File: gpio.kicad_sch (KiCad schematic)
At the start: 13 parts, among them J5 Conn_02x08_Odd_Even, J6 USB_9P, J7 Conn_01x04, U10 TLP172GM, U5 TLP172GM, U6 TLP172GM, U9 TLP172GM

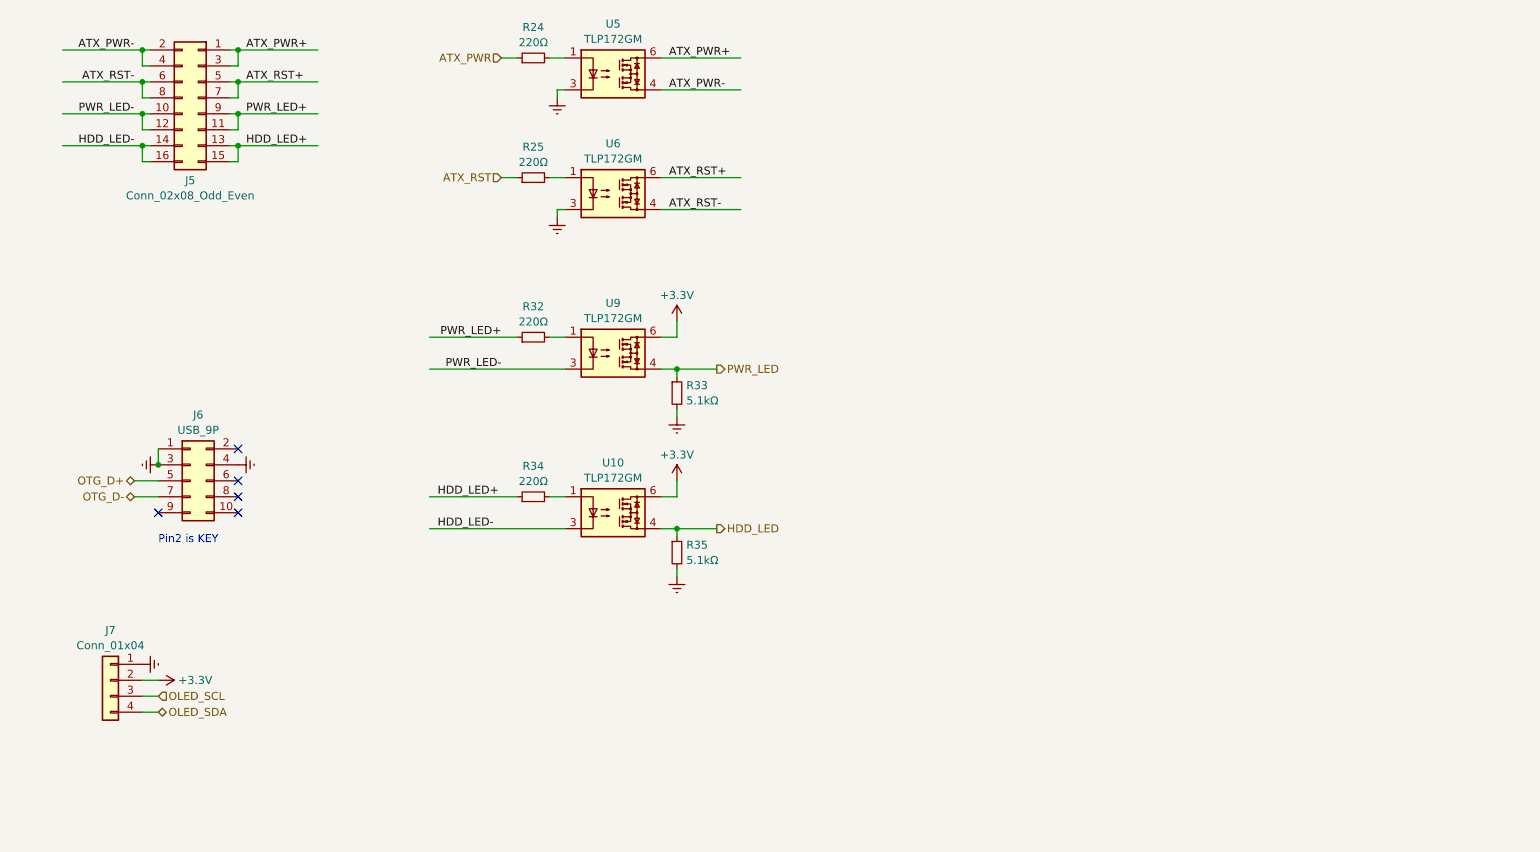
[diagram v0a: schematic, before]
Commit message: Update pcb & sch for T113 SOM
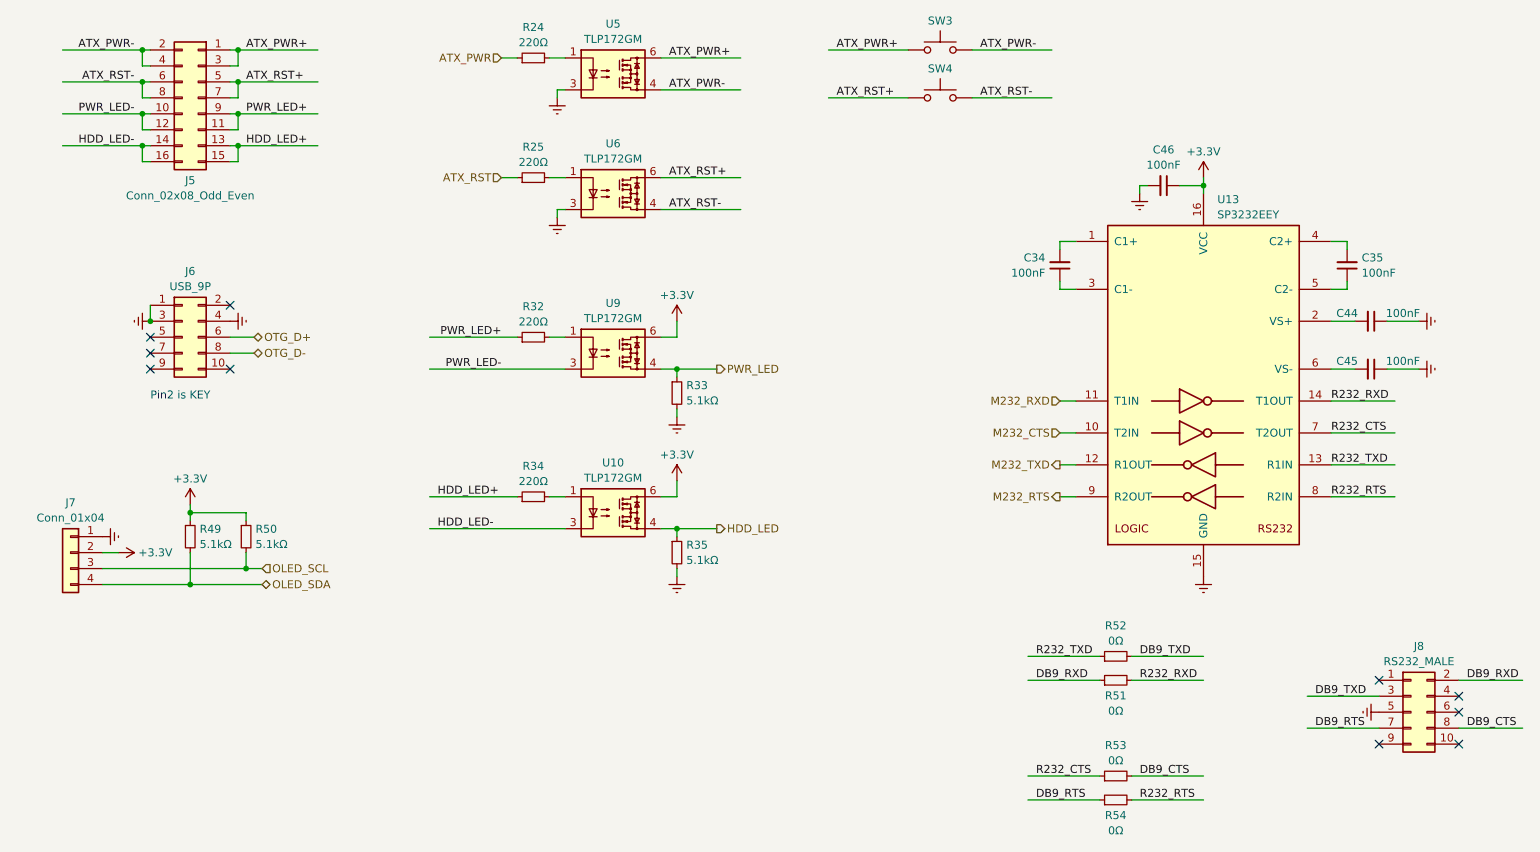
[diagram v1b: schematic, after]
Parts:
- added C34, C35, C44, C45, C46: 100nF, Capacitor_SMD:C_0402_1005Metric, symbol Device:C_Small
- added J8: RS232_MALE, easyeda2kicad:IDC-SMD_10P-P2.54-V-R2-C5-S9.50, symbol Connector_Generic:Conn_02x05_Odd_Even
- added R49, R50: 5.1kΩ, Resistor_SMD:R_0402_1005Metric, symbol Device:R_Small
- added R51, R52, R53, R54: 0Ω, Resistor_SMD:R_0402_1005Metric, symbol Device:R_Small
- added SW3, SW4: TS-1187A, Button_Switch_SMD:SW_Push_1P1T_XKB_TS-1187A, symbol Switch:SW_Push
- added U13: SP3232EEY, Package_SO:TSSOP-16_4.4x5mm_P0.65mm, symbol Interface_UART:MAX3232
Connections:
- net +3.3V: now also C46.1, R49.1, R50.1, U13.16 (VCC)
- net ATX_PWR+: now also SW3.1
- net ATX_PWR-: now also SW3.2
- net ATX_RST+: now also SW4.1
- net ATX_RST-: now also SW4.2
- net Earth: now also C44.1, C45.1, C46.2, J8.5 (Pin_5), U13.15 (GND)
- net OLED_SCL: now also R50.2
- net OLED_SDA: now also R49.2
- net OTG_D+: now also J6.6 (Pin_6); no longer J6.5 (Pin_5)
- net OTG_D-: now also J6.8 (Pin_8); no longer J6.7 (Pin_7)
- new net: C45.2, U13.6 (VS-)
- new net: C34.2, U13.1 (C1+)
- new net: C44.2, U13.2 (VS+)
- new net: C34.1, U13.3 (C1-)
- new net: C35.2, U13.4 (C2+)
- new net: C35.1, U13.5 (C2-)
- new net DB9_CTS: J8.8 (Pin_8), R53.2
- new net DB9_RTS: J8.7 (Pin_7), R54.1
- new net DB9_RXD: J8.2 (Pin_2), R51.1
- new net DB9_TXD: J8.3 (Pin_3), R52.2
- new net M232_CTS: U13.10 (T2IN)
- new net M232_RTS: U13.9 (R2OUT)
- new net M232_RXD: U13.11 (T1IN)
- new net M232_TXD: U13.12 (R1OUT)
- new net R232_CTS: R53.1, U13.7 (T2OUT)
- new net R232_RTS: R54.2, U13.8 (R2IN)
- new net R232_RXD: R51.2, U13.14 (T1OUT)
- new net R232_TXD: R52.1, U13.13 (R1IN)
- no-connect marks 5 -> 10
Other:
- moved on the sheet: J6, J7

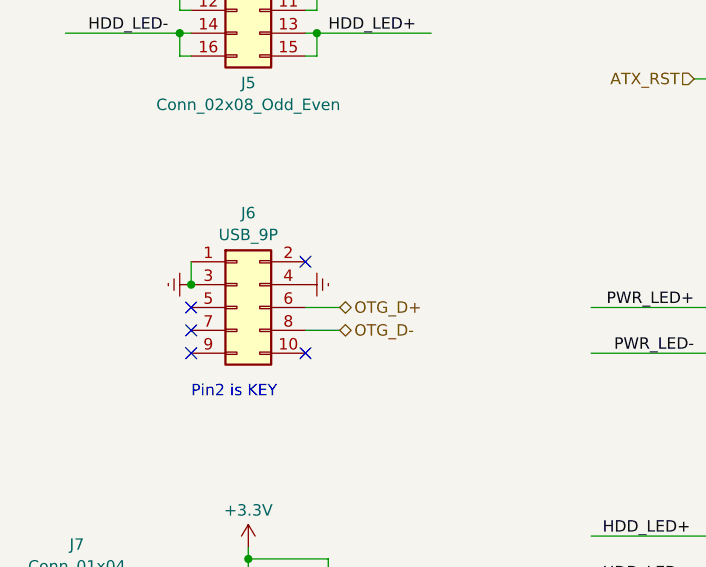
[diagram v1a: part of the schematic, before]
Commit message: Fix MS2109 symbol power pins, initial v1 release
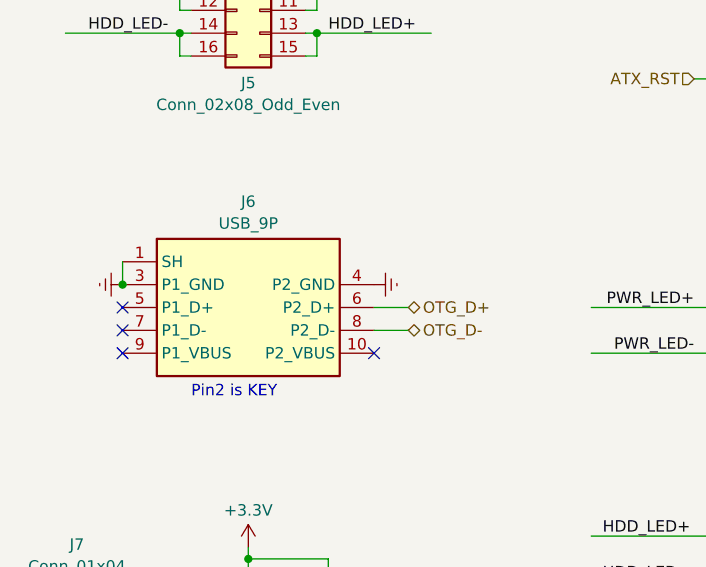
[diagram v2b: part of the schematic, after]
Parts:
- J6: symbol Connector_Generic:Conn_02x05_Odd_Even -> tukvm:PinHeader_USB_2.0_9Pin
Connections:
- no-connect marks 10 -> 9
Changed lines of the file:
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@@
 	(paper "A4")
 	(junction
-		(at 49.53 72.39)
-		(diameter 0)
-		(color 0 0 0 0)
-	)
-	(junction
 		(at 63.5 34.29)
 		(diameter 0)
@@
 	)
 	(junction
+		(at 41.91 72.39)
+		(diameter 0)
+		(color 0 0 0 0)
+	)
+	(junction
 		(at 48.26 29.21)
 		(diameter 0)
@@
 	)
 	(no_connect
-		(at 62.23 69.85)
-	)
-	(no_connect
 		(at 257.81 132.08)
 	)
 	(no_connect
-		(at 62.23 80.01)
+		(at 69.85 80.01)
 	)
 	(no_connect
@@
 	)
 	(no_connect
-		(at 49.53 80.01)
+		(at 41.91 80.01)
 	)
 	(no_connect
@@
 	)
 	(no_connect
-		(at 49.53 74.93)
+		(at 41.91 74.93)
 	)
 	(no_connect
@@
 	)
 	(no_connect
-		(at 49.53 77.47)
+		(at 41.91 77.47)
 	)
 	(wire
@@
 	(wire
 		(pts
-			(xy 49.53 69.85) (xy 49.53 72.39)
+			(xy 41.91 69.85) (xy 41.91 72.39)
 		)
 		(stroke
@@
 	(wire
 		(pts
-			(xy 66.04 74.93) (xy 62.23 74.93)
+			(xy 73.66 74.93) (xy 69.85 74.93)
 		)
 		(stroke
@@
 	(wire
 		(pts
-			(xy 66.04 77.47) (xy 62.23 77.47)
+			(xy 73.66 77.47) (xy 69.85 77.47)
 		)
 		(stroke
@@
 	(hierarchical_label "OTG_D-"
 		(shape bidirectional)
-		(at 66.04 77.47 0)
+		(at 73.66 77.47 0)
 		(fields_autoplaced yes)
 		(effects
@@
 	(hierarchical_label "OTG_D+"
 		(shape bidirectional)
-		(at 66.04 74.93 0)
+		(at 73.66 74.93 0)
 		(fields_autoplaced yes)
 		(effects
@@
 	(symbol
 		(lib_id "power:Earth")
-		(at 62.23 72.39 90)
+		(at 69.85 72.39 90)
 		(unit 1)
 		(exclude_from_sim no)
@@
 		(dnp no)
 		(property "Reference" "#PWR081"
-			(at 68.58 72.39 0)
+			(at 76.2 72.39 0)
 			(effects
 				(font
@@
 		)
 		(property "Value" "Earth"
-			(at 66.04 72.39 0)
+			(at 73.66 72.39 0)
 			(effects
 				(font
@@
 		)
 		(property "Footprint" ""
-			(at 62.23 72.39 0)
+			(at 69.85 72.39 0)
 			(effects
 				(font
@@
 		)
 		(property "Datasheet" "~"
-			(at 62.23 72.39 0)
+			(at 69.85 72.39 0)
 			(effects
 				(font
@@
 		)
 		(property "Description" ""
-			(at 62.23 72.39 0)
+			(at 69.85 72.39 0)
 			(effects
 				(font
@@
 	(symbol
 		(lib_id "power:Earth")
-		(at 49.53 72.39 270)
+		(at 41.91 72.39 270)
 		(unit 1)
 		(exclude_from_sim no)
@@
 		(dnp no)
 		(property "Reference" "#PWR079"
-			(at 43.18 72.39 0)
+			(at 35.56 72.39 0)
 			(effects
 				(font
@@
 		)
 		(property "Value" "Earth"
-			(at 45.72 72.39 0)
+			(at 38.1 72.39 0)
 			(effects
 				(font
@@
 		)
 		(property "Footprint" ""
-			(at 49.53 72.39 0)
+			(at 41.91 72.39 0)
 			(effects
 				(font
@@
 		)
 		(property "Datasheet" "~"
-			(at 49.53 72.39 0)
+			(at 41.91 72.39 0)
 			(effects
 				(font
@@
 		)
 		(property "Description" ""
-			(at 49.53 72.39 0)
+			(at 41.91 72.39 0)
 			(effects
 				(font
@@
 	)
 	(symbol
-		(lib_id "Connector_Generic:Conn_02x05_Odd_Even")
-		(at 54.61 74.93 0)
+		(lib_id "tukvm:PinHeader_USB_2.0_9Pin")
+		(at 55.88 74.93 0)
 		(unit 1)
 		(exclude_from_sim no)
@@
 		(fields_autoplaced yes)
 		(property "Reference" "J6"
-			(at 55.88 64.4357 0)
+			(at 55.88 63.1655 0)
 			(effects
 				(font
@@
 		)
 		(property "Value" "USB_9P"
-			(at 55.88 66.8599 0)
+			(at 55.88 65.5898 0)
 			(effects
 				(font
@@
 		)
 		(property "Footprint" "tukvm:USB_9P_P2.54mm_Horizontal"
-			(at 54.61 74.93 0)
+			(at 55.88 74.93 0)
 			(effects
 				(font
@@
 		)
 		(property "Datasheet" "~"
-			(at 54.61 74.93 0)
+			(at 46.99 74.93 0)
 			(effects
 				(font
@@
 		)
 		(property "Description" ""
-			(at 54.61 74.93 0)
+			(at 46.99 74.93 0)
 			(effects
 				(font
@@
 		(pin "8"
 		)
-		(pin "2"
-		)
 		(pin "7"

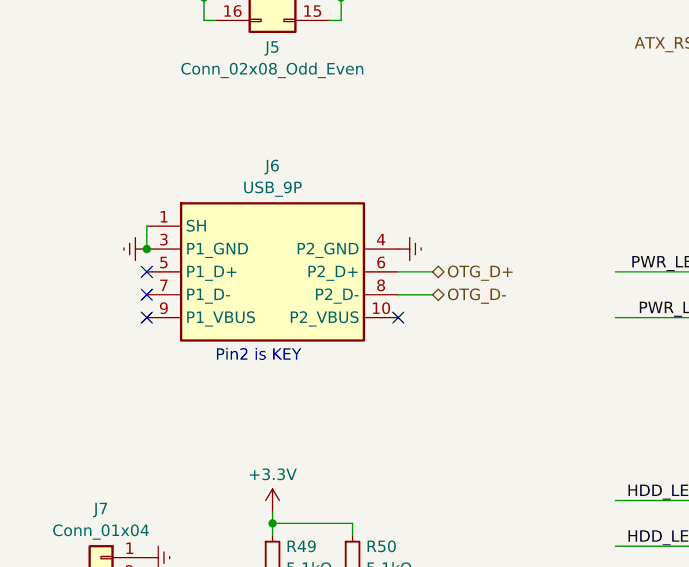
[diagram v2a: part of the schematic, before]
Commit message: Fix OTG USB polarity
Signed-off-by: Yichuan Gao <gaoyichuan000@gmail.com>
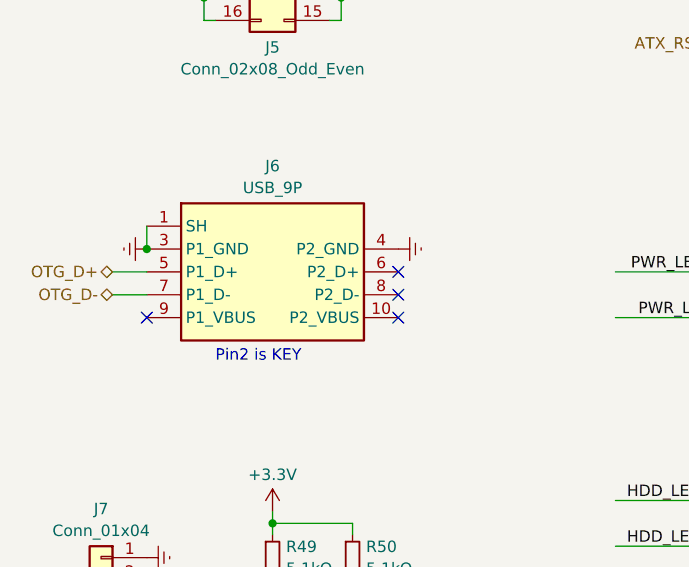
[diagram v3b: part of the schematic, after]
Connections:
- net OTG_D+: now also J6.5 (P1_D+); no longer J6.6 (P2_D+)
- net OTG_D-: now also J6.7 (P1_D-); no longer J6.8 (P2_D-)
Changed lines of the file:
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@@
 	)
 	(no_connect
-		(at 41.91 74.93)
+		(at 69.85 74.93)
 	)
 	(no_connect
@@
 	)
 	(no_connect
-		(at 41.91 77.47)
+		(at 69.85 77.47)
 	)
 	(wire
@@
 	(wire
 		(pts
+			(xy 38.1 77.47) (xy 41.91 77.47)
+		)
+		(stroke
+			(width 0)
+			(type default)
+		)
+	)
+	(wire
+		(pts
 			(xy 237.49 90.17) (xy 247.65 90.17)
 		)
@@
 	(wire
 		(pts
+			(xy 38.1 74.93) (xy 41.91 74.93)
+		)
+		(stroke
+			(width 0)
+			(type default)
+		)
+	)
+	(wire
+		(pts
 			(xy 48.26 39.37) (xy 49.53 39.37)
 		)
@@
 	(wire
 		(pts
-			(xy 73.66 74.93) (xy 69.85 74.93)
-		)
-		(stroke
-			(width 0)
-			(type default)
-		)
-	)
-	(wire
-		(pts
 			(xy 205.74 144.78) (xy 217.17 144.78)
 		)
@@
 		(pts
 			(xy 257.81 129.54) (xy 267.97 129.54)
-		)
-		(stroke
-			(width 0)
-			(type default)
-		)
-	)
-	(wire
-		(pts
-			(xy 73.66 77.47) (xy 69.85 77.47)
 		)
 		(stroke
@@
 		)
 	)
+	(hierarchical_label "OTG_D+"
+		(shape bidirectional)
+		(at 38.1 74.93 180)
+		(fields_autoplaced yes)
+		(effects
+			(font
+				(size 1.27 1.27)
+			)
+			(justify right)
+		)
+	)
 	(hierarchical_label "OTG_D-"
 		(shape bidirectional)
-		(at 73.66 77.47 0)
-		(fields_autoplaced yes)
-		(effects
-			(font
-				(size 1.27 1.27)
-			)
-			(justify left)
-		)
-	)
-	(hierarchical_label "OTG_D+"
-		(shape bidirectional)
-		(at 73.66 74.93 0)
-		(fields_autoplaced yes)
-		(effects
-			(font
-				(size 1.27 1.27)
-			)
-			(justify left)
-		)
-	)
+		(at 38.1 77.47 180)
+		(fields_autoplaced yes)
+		(effects
+			(font
+				(size 1.27 1.27)
+			)
+			(justify right)
+		)
+	)
